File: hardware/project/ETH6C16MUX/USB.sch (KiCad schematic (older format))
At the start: 9 parts

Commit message: Schematic design
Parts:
- L?: symbol ETH6C12MUX:744233121 -> ETH6C16MUX:744233121
- U?: symbol ETH6C12MUX:824011 -> ETH6C16MUX:824011
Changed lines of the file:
@@
 EESchema Schematic File Version 4
-LIBS:ETH6C12MUX-cache
+LIBS:ETH6C16MUX-cache
 EELAYER 30 0
 EELAYER END
@@
 	4000 1950 4000 1900
 $Comp
-L ETH6C12MUX:744233121 L?
+L ETH6C16MUX:744233121 L?
 U 1 1 5D613F1C
 P 5000 2850
@@
 	4800 2750 4150 2750
 $Comp
-L ETH6C12MUX:824011 U?
+L ETH6C16MUX:824011 U?
 U 1 1 5D6092DD
 P 6700 4100
@@
 	6200 1900 6200 1950
 $Comp
-L ETH6C12MUX:V_USB2 #PWR?
+L ETH6C16MUX:V_USB2 #PWR?
 U 1 1 5D64A71D
 P 6700 3800
@@
 	6200 3000 6200 3150
 $Comp
-L ETH6C12MUX:+5V_USB1 #PWR?
+L ETH6C16MUX:+5V_USB1 #PWR?
 U 1 1 5D6B2E7A
 P 4000 1900
@@
 $EndComp
 $Comp
-L ETH6C12MUX:V_USB1 #PWR?
+L ETH6C16MUX:V_USB1 #PWR?
 U 1 1 5D6B3D26
 P 6200 1900

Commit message: USB update
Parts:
- removed R?: 0, symbol Device:R
- added C? (x2): 1u, symbol Device:C
- added C?: 100n, symbol Device:C
- added R? (x2): 27, symbol Device:R
- added R?: 10k, symbol Device:R
- added U?: FT230XQ, Package_DFN_QFN:QFN-16-1EP_4x4mm_P0.65mm_EP2.1x2.1mm, symbol Interface_USB:FT230XQ
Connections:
- net labels added: +5V, +5V_USB, F_USB_D+, F_USB_D-, GND, MCU_RX_UART3, MCU_TX_UART3
- net labels removed: +5V_USB1, USB_ID, USB_VBUS, V_USB1, V_USB2
- wire segments 40 -> 57
- no-connect marks 0 -> 7
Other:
- moved on the sheet: C?, D?, J?, L?, R?, U?

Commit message: Schematic design
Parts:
- C504: renamed from C?; footprint (none) -> ETH6C16MXU:C_0603_A_Pad1.05x0.95mm_HandSolder
- D501: renamed from D?; value D_Schottky -> CUS08F30; footprint (none) -> Diode_SMD:D_SOD-323_HandSoldering
- J501: renamed from J?; footprint (none) -> Connector_USB:USB_Micro-B_Molex-105133-0001
- R501: renamed from R?; value R -> 0/2W
- R502, R503: renamed from R?; footprint (none) -> Resistor_SMD:R_0603_1608Metric_Pad1.05x0.95mm_HandSolder
- U502: renamed from U?; footprint (none) -> Package_TO_SOT_SMD:SOT-23-5
- gave numbers to parts that had none: 8
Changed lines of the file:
@@
 $Descr A4 11693 8268
 encoding utf-8
-Sheet 5 8
+Sheet 5 9
 Title "USB"
 Date ""
@@
 	6650 3500 6200 3500
 $Comp
-L Device:R R?
+L Device:R R503
 U 1 1 5D6EAF5C
 P 6800 3500
-F 0 "R?" V 6700 3500 50  0000 C CNN
+F 0 "R503" V 6700 3500 50  0000 C CNN
 F 1 "27" V 6800 3500 50  0000 C CNN
-F 2 "" V 6730 3500 50  0001 C CNN
+F 2 "Resistor_SMD:R_0603_1608Metric_Pad1.05x0.95mm_HandSolder" V 6730 3500 50  0001 C CNN
 F 3 "~" H 6800 3500 50  0001 C CNN
 	1    6800 3500
@@
 	6650 3300 6200 3300
 $Comp
-L Device:R R?
+L Device:R R502
 U 1 1 5D6EA732
 P 6800 3300
-F 0 "R?" V 6700 3300 50  0000 C CNN
+F 0 "R502" V 6700 3300 50  0000 C CNN
 F 1 "27" V 6800 3300 50  0000 C CNN
-F 2 "" V 6730 3300 50  0001 C CNN
+F 2 "Resistor_SMD:R_0603_1608Metric_Pad1.05x0.95mm_HandSolder" V 6730 3300 50  0001 C CNN
 F 3 "~" H 6800 3300 50  0001 C CNN
 	1    6800 3300
@@
 	7700 3450 7900 3450
 $Comp
-L power:GNDD #PWR?
+L power:GNDD #PWR0511
 U 1 1 5D614548
 P 9050 5000
-F 0 "#PWR?" H 9050 4750 50  0001 C CNN
+F 0 "#PWR0511" H 9050 4750 50  0001 C CNN
 F 1 "GNDD" H 9054 4845 50  0000 C CNN
 F 2 "" H 9050 5000 50  0001 C CNN
@@
 $EndComp
 $Comp
-L ETH6C16MUX:824011 U?
+L ETH6C16MUX:824011 U502
 U 1 1 5D6092DD
 P 9050 4650
-F 0 "U?" H 9328 4671 50  0000 L CNN
+F 0 "U502" H 9328 4671 50  0000 L CNN
 F 1 "824011" H 9328 4580 50  0000 L CNN
-F 2 "" H 8800 4650 50  0001 C CNN
+F 2 "Package_TO_SOT_SMD:SOT-23-5" H 8800 4650 50  0001 C CNN
 F 3 "" H 8800 4650 50  0001 C CNN
 	1    9050 4650
@@
 	7700 3450 7700 3500
 $Comp
-L ETH6C16MUX:744233121 L?
+L ETH6C16MUX:744233121 L502
 U 1 1 5D613F1C
 P 7350 3400
-F 0 "L?" H 7350 3600 50  0000 C CNN
+F 0 "L502" H 7350 3600 50  0000 C CNN
 F 1 "744233121" H 7350 3200 50  0000 C CNN
 F 2 "" H 7350 3400 50  0001 C CNN
@@
 $EndComp
 $Comp
-L Connector:USB_B_Micro J?
+L Connector:USB_B_Micro J501
 U 1 1 5D762E84
 P 9000 3350
-F 0 "J?" H 9057 3817 50  0000 C CNN
+F 0 "J501" H 9057 3817 50  0000 C CNN
 F 1 "105133-0001" H 9057 3726 50  0000 C CNN
-F 2 "" H 9150 3300 50  0001 C CNN
+F 2 "Connector_USB:USB_Micro-B_Molex-105133-0001" H 9150 3300 50  0001 C CNN
 F 3 "~" H 9150 3300 50  0001 C CNN
 	1    9000 3350
@@
 	9000 3800 9000 3750
 $Comp
-L power:GNDD #PWR?
+L power:GNDD #PWR0507
 U 1 1 5D768FA3
 P 9050 3850
-F 0 "#PWR?" H 9050 3600 50  0001 C CNN
+F 0 "#PWR0507" H 9050 3600 50  0001 C CNN
 F 1 "GNDD" H 9054 3695 50  0000 C CNN
 F 2 "" H 9050 3850 50  0001 C CNN
@@
 	6900 2150 6700 2150
 $Comp
-L Device:R R?
+L Device:R R501
 U 1 1 5DBF6D03
 P 7050 2150
-F 0 "R?" V 6843 2150 50  0000 C CNN
-F 1 "R" V 6934 2150 50  0000 C CNN
+F 0 "R501" V 6843 2150 50  0000 C CNN
+F 1 "0/2W" V 6934 2150 50  0000 C CNN
 F 2 "" V 6980 2150 50  0001 C CNN
 F 3 "~" H 7050 2150 50  0001 C CNN
@@
 $EndComp
 $Comp
-L Device:D_Schottky D?
+L Device:D_Schottky D501
 U 1 1 5DBF3C7F
 P 7050 2500
-F 0 "D?" H 7050 2716 50  0000 C CNN
-F 1 "D_Schottky" H 7050 2625 50  0000 C CNN
-F 2 "" H 7050 2500 50  0001 C CNN
+F 0 "D501" H 7050 2716 50  0000 C CNN
+F 1 "CUS08F30" H 7050 2625 50  0000 C CNN
+F 2 "Diode_SMD:D_SOD-323_HandSoldering" H 7050 2500 50  0001 C CNN
 F 3 "~" H 7050 2500 50  0001 C CNN
 	1    7050 2500
@@
 Connection ~ 8050 2500
 $Comp
-L power:GNDD #PWR?
+L power:GNDD #PWR0504
 U 1 1 5D600B45
 P 8050 2850
-F 0 "#PWR?" H 8050 2600 50  0001 C CNN
+F 0 "#PWR0504" H 8050 2600 50  0001 C CNN
 F 1 "GNDD" H 8054 2695 50  0000 C CNN
 F 2 "" H 8050 2850 50  0001 C CNN
@@
 $EndComp
 $Comp
-L power:GNDD #PWR?
+L power:GNDD #PWR0503
 U 1 1 5D600B3F
 P 7450 2850
-F 0 "#PWR?" H 7450 2600 50  0001 C CNN
+F 0 "#PWR0503" H 7450 2600 50  0001 C CNN
 F 1 "GNDD" H 7454 2695 50  0000 C CNN
 F 2 "" H 7450 2850 50  0001 C CNN
@@
 	8050 2550 8050 2500
 $Comp
-L Device:CP C?
+L Device:CP C502
 U 1 1 5D600B35
 P 8050 2700
-F 0 "C?" H 8168 2746 50  0000 L CNN
+F 0 "C502" H 8168 2746 50  0000 L CNN
 F 1 "470u" H 8168 2655 50  0000 L CNN
 F 2 "" H 8088 2550 50  0001 C CNN
@@
 $EndComp
 $Comp
-L Device:L L?
+L Device:L L501
 U 1 1 5D600B2F
 P 7750 2500
-F 0 "L?" V 7940 2500 50  0000 C CNN
+F 0 "L501" V 7940 2500 50  0000 C CNN
 F 1 "744053220" V 7849 2500 50  0000 C CNN
 F 2 "" H 7750 2500 50  0001 C CNN
@@
 $EndComp
 $Comp
-L Device:CP C?
+L Device:CP C501
 U 1 1 5D600B29
 P 7450 2700
-F 0 "C?" H 7568 2746 50  0000 L CNN
+F 0 "C501" H 7568 2746 50  0000 L CNN
 F 1 "470u" H 7568 2655 50  0000 L CNN
 F 2 "" H 7488 2550 50  0001 C CNN
@@
 NoConn ~ 8700 3550
 $Comp
-L Interface_USB:FT230XQ U?
+L Interface_USB:FT230XQ U501
 U 1 1 5D6F3A21
 P 3800 3650
-F 0 "U?" H 3400 4350 50  0000 C CNN
+F 0 "U501" H 3400 4350 50  0000 C CNN
 F 1 "FT230XQ" H 3400 4250 50  0000 C CNN
 F 2 "Package_DFN_QFN:QFN-16-1EP_4x4mm_P0.65mm_EP2.1x2.1mm" H 4350 2950 50  0001 C CNN
@@
 	4850 3650 4500 3650
 $Comp
-L Device:C C?
+L Device:C C505
 U 1 1 5D71767C
 P 1600 7100
-F 0 "C?" H 1715 7146 50  0000 L CNN
+F 0 "C505" H 1715 7146 50  0000 L CNN
 F 1 "1u" H 1715 7055 50  0000 L CNN
 F 2 "" H 1638 6950 50  0001 C CNN
@@
 	3800 4400 3900 4400
 $Comp
-L power:GND #PWR?
+L power:GND #PWR0510
 U 1 1 5D71A5DB
 P 3800 4450
-F 0 "#PWR?" H 3800 4200 50  0001 C CNN
+F 0 "#PWR0510" H 3800 4200 50  0001 C CNN
 F 1 "GND" H 3805 4277 50  0000 C CNN
 F 2 "" H 3800 4450 50  0001 C CNN
@@
 	3700 2550 3700 2950
 $Comp
-L Device:R R?
+L Device:R R504
 U 1 1 5D7279EC
 P 5000 3600
-F 0 "R?" H 4930 3554 50  0000 R CNN
+F 0 "R504" H 4930 3554 50  0000 R CNN
 F 1 "10k" H 4930 3645 50  0000 R CNN
 F 2 "" V 4930 3600 50  0001 C CNN
@@
 Connection ~ 5000 3250
 $Comp
-L Device:C C?
+L Device:C C504
 U 1 1 5D72EA0B
 P 5000 4100
-F 0 "C?" H 5115 4146 50  0000 L CNN
+F 0 "C504" H 5115 4146 50  0000 L CNN
 F 1 "100n" H 5115 4055 50  0000 L CNN
-F 2 "" H 5038 3950 50  0001 C CNN
+F 2 "ETH6C16MXU:C_0603_A_Pad1.05x0.95mm_HandSolder" H 5038 3950 50  0001 C CNN
 F 3 "~" H 5000 4100 50  0001 C CNN
 	1    5000 4100
@@
 Connection ~ 5000 3850
 $Comp
-L power:GND #PWR?
+L power:GND #PWR0508
 U 1 1 5D7314EE
 P 5000 4250
-F 0 "#PWR?" H 5000 4000 50  0001 C CNN
+F 0 "#PWR0508" H 5000 4000 50  0001 C CNN
 F 1 "GND" H 5005 4077 50  0000 C CNN
 F 2 "" H 5000 4250 50  0001 C CNN
@@
 $EndComp
 $Comp
-L Device:C C?
+L Device:C C503
 U 1 1 5D73543E
 P 4550 2750
-F 0 "C?" H 4665 2796 50  0000 L CNN
+F 0 "C503" H 4665 2796 50  0000 L CNN
 F 1 "1u" H 4665 2705 50  0000 L CNN
 F 2 "" H 4588 2600 50  0001 C CNN
@@
 	4550 2550 3700 2550
 $Comp
-L power:GND #PWR?
+L power:GND #PWR0505
 U 1 1 5D739887
 P 4550 2900
-F 0 "#PWR?" H 4550 2650 50  0001 C CNN
+F 0 "#PWR0505" H 4550 2650 50  0001 C CNN
 F 1 "GND" H 4555 2727 50  0000 C CNN
 F 2 "" H 4550 2900 50  0001 C CNN
@@
 NoConn ~ 3100 3550
 $Comp
-L power:GND #PWR?
+L power:GND #PWR0513
 U 1 1 5D76832A
 P 1600 7250
-F 0 "#PWR?" H 1600 7000 50  0001 C CNN
+F 0 "#PWR0513" H 1600 7000 50  0001 C CNN
 F 1 "GND" H 1605 7077 50  0000 C CNN
 F 2 "" H 1600 7250 50  0001 C CNN
@@
 MCU_RX_UART3
 $Comp
-L power:+5V #PWR?
+L power:+5V #PWR0501
 U 1 1 5D78D21A
 P 6350 2450
-F 0 "#PWR?" H 6350 2300 50  0001 C CNN
+F 0 "#PWR0501" H 6350 2300 50  0001 C CNN
 F 1 "+5V" H 6365 2623 50  0000 C CNN
 F 2 "" H 6350 2450 50  0001 C CNN
@@
 $EndComp
 $Comp
-L ETH6C16MUX:+5V_USB #PWR?
+L ETH6C16MUX:+5V_USB #PWR0502
 U 1 1 5D78DEBD
 P 8550 2450
-F 0 "#PWR?" H 8550 2300 50  0001 C CNN
+F 0 "#PWR0502" H 8550 2300 50  0001 C CNN
 F 1 "+5V_USB" H 8565 2623 50  0000 C CNN
 F 2 "" H 8550 2450 50  0001 C CNN
@@
 $EndComp
 $Comp
-L ETH6C16MUX:+5V_USB #PWR?
+L ETH6C16MUX:+5V_USB #PWR0509
 U 1 1 5D78E0EA
 P 9050 4350
-F 0 "#PWR?" H 9050 4200 50  0001 C CNN
+F 0 "#PWR0509" H 9050 4200 50  0001 C CNN
 F 1 "+5V_USB" H 9065 4523 50  0000 C CNN
 F 2 "" H 9050 4350 50  0001 C CNN
@@
 $EndComp
 $Comp
-L power:+5V #PWR?
+L power:+5V #PWR0506
 U 1 1 5D7913F2
 P 3900 2950
-F 0 "#PWR?" H 3900 2800 50  0001 C CNN
+F 0 "#PWR0506" H 3900 2800 50  0001 C CNN
 F 1 "+5V" H 3915 3123 50  0000 C CNN
 F 2 "" H 3900 2950 50  0001 C CNN
@@
 $EndComp
 $Comp
-L power:+5V #PWR?
+L power:+5V #PWR0512
 U 1 1 5D7940E4
 P 1600 6950
-F 0 "#PWR?" H 1600 6800 50  0001 C CNN
+F 0 "#PWR0512" H 1600 6800 50  0001 C CNN
 F 1 "+5V" H 1615 7123 50  0000 C CNN
 F 2 "" H 1600 6950 50  0001 C CNN

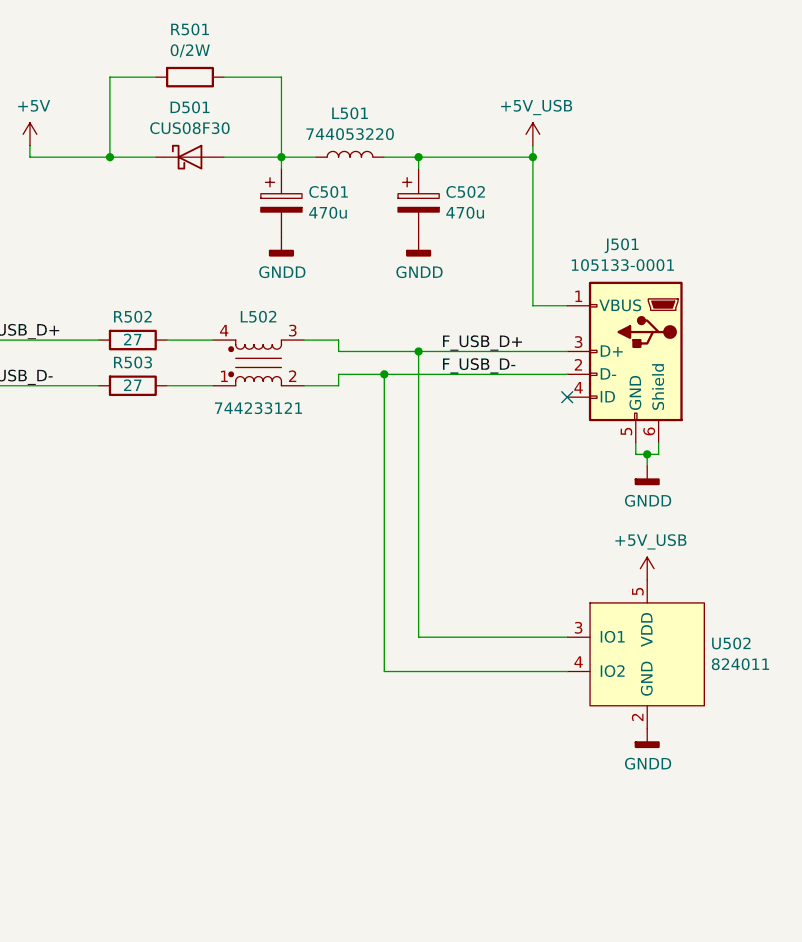
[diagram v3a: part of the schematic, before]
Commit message: PCB design, need to redesign of the board to board connectors.
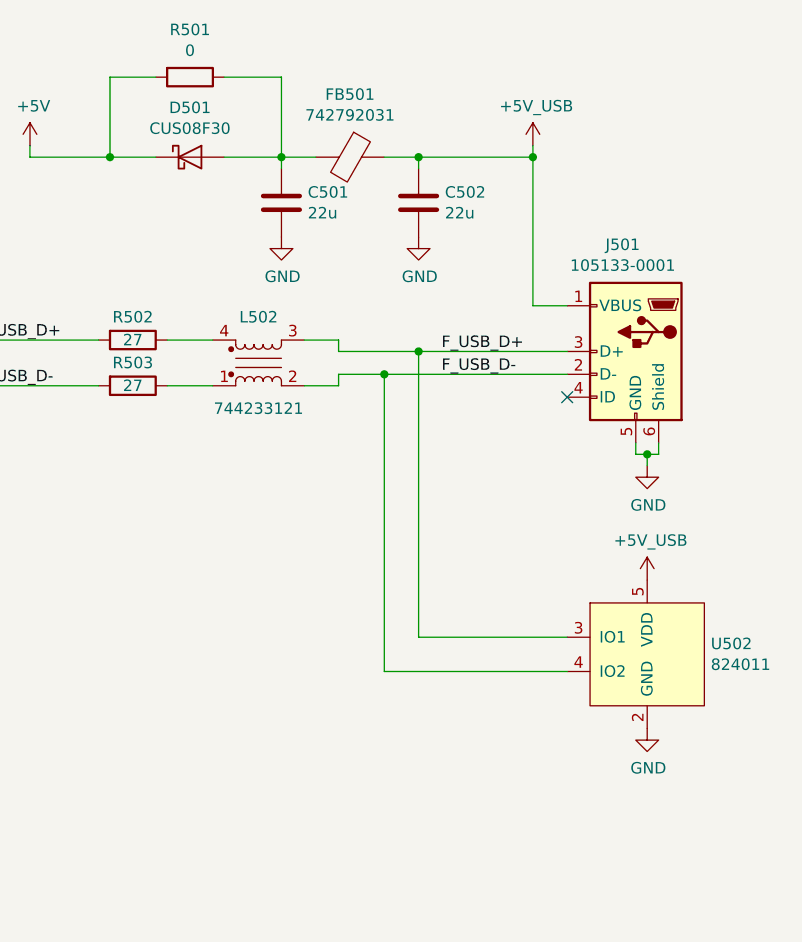
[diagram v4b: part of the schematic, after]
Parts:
- removed C501, C502: 470u, symbol Device:CP
- removed L501: 744053220, symbol Device:L
- added C501, C502: 22u, ETH6C16MXU:C_1210_BB_3225Metric_Pad1.42x2.65mm_HandSolder, symbol Device:C
- added FB501: 742792031, ETH6C16MXU:R_0805_D_Pad1.15x1.40mm_HandSolder, symbol Device:Ferrite_Bead
- C503, C505: footprint (none) -> ETH6C16MXU:C_0603_B_Pad1.05x0.95mm_HandSolder
- L502: footprint (none) -> ETH6C16MXU:744233121
- R501: value 0/2W -> 0; footprint (none) -> Resistor_SMD:R_0612_1632Metric_Pad1.18x3.40mm_HandSolder
- R504: footprint (none) -> ETH6C16MXU:R_0603_E_Pad1.05x0.95mm_HandSolder
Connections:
- net GNDD is gone; now on net GND: J501.5 (GND), J501.6 (Shield), U502.2 (GND)
- net +5V_USB: now also C502.1, FB501.1
- net GND: now also C501.2, C502.2
- net at D501.2 (A), R501.1: now also C501.1, FB501.2
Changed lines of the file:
@@
 	7700 3450 7900 3450
-$Comp
-L power:GNDD #PWR0511
-U 1 1 5D614548
-P 9050 5000
-F 0 "#PWR0511" H 9050 4750 50  0001 C CNN
-F 1 "GNDD" H 9054 4845 50  0000 C CNN
-F 2 "" H 9050 5000 50  0001 C CNN
-F 3 "" H 9050 5000 50  0001 C CNN
-	1    9050 5000
-	1    0    0    -1
-$EndComp
 $Comp
 L ETH6C16MUX:824011 U502
@@
 F 0 "L502" H 7350 3600 50  0000 C CNN
 F 1 "744233121" H 7350 3200 50  0000 C CNN
-F 2 "" H 7350 3400 50  0001 C CNN
+F 2 "ETH6C16MXU:744233121" H 7350 3400 50  0001 C CNN
 F 3 "" H 7350 3400 50  0001 C CNN
 	1    7350 3400
@@
 Wire Wire Line
 	9000 3800 9000 3750
-$Comp
-L power:GNDD #PWR0507
-U 1 1 5D768FA3
-P 9050 3850
-F 0 "#PWR0507" H 9050 3600 50  0001 C CNN
-F 1 "GNDD" H 9054 3695 50  0000 C CNN
-F 2 "" H 9050 3850 50  0001 C CNN
-F 3 "" H 9050 3850 50  0001 C CNN
-	1    9050 3850
-	1    0    0    -1
-$EndComp
 Wire Wire Line
 	9050 3850 9050 3800
@@
 P 7050 2150
 F 0 "R501" V 6843 2150 50  0000 C CNN
-F 1 "0/2W" V 6934 2150 50  0000 C CNN
-F 2 "" V 6980 2150 50  0001 C CNN
+F 1 "0" V 6934 2150 50  0000 C CNN
+F 2 "Resistor_SMD:R_0612_1632Metric_Pad1.18x3.40mm_HandSolder" V 6980 2150 50  0001 C CNN
 F 3 "~" H 7050 2150 50  0001 C CNN
 	1    7050 2150
@@
 	6700 2500 6350 2500
 Connection ~ 8050 2500
-$Comp
-L power:GNDD #PWR0504
-U 1 1 5D600B45
-P 8050 2850
-F 0 "#PWR0504" H 8050 2600 50  0001 C CNN
-F 1 "GNDD" H 8054 2695 50  0000 C CNN
-F 2 "" H 8050 2850 50  0001 C CNN
-F 3 "" H 8050 2850 50  0001 C CNN
-	1    8050 2850
-	1    0    0    -1
-$EndComp
-$Comp
-L power:GNDD #PWR0503
-U 1 1 5D600B3F
-P 7450 2850
-F 0 "#PWR0503" H 7450 2600 50  0001 C CNN
-F 1 "GNDD" H 7454 2695 50  0000 C CNN
-F 2 "" H 7450 2850 50  0001 C CNN
-F 3 "" H 7450 2850 50  0001 C CNN
-	1    7450 2850
-	1    0    0    -1
-$EndComp
 Wire Wire Line
 	7450 2500 7450 2550
@@
 Wire Wire Line
 	8050 2550 8050 2500
-$Comp
-L Device:CP C502
-U 1 1 5D600B35
-P 8050 2700
-F 0 "C502" H 8168 2746 50  0000 L CNN
-F 1 "470u" H 8168 2655 50  0000 L CNN
-F 2 "" H 8088 2550 50  0001 C CNN
-F 3 "~" H 8050 2700 50  0001 C CNN
-	1    8050 2700
-	1    0    0    -1
-$EndComp
-$Comp
-L Device:L L501
-U 1 1 5D600B2F
-P 7750 2500
-F 0 "L501" V 7940 2500 50  0000 C CNN
-F 1 "744053220" V 7849 2500 50  0000 C CNN
-F 2 "" H 7750 2500 50  0001 C CNN
-F 3 "~" H 7750 2500 50  0001 C CNN
-	1    7750 2500
-	0    -1   -1   0
-$EndComp
-$Comp
-L Device:CP C501
-U 1 1 5D600B29
-P 7450 2700
-F 0 "C501" H 7568 2746 50  0000 L CNN
-F 1 "470u" H 7568 2655 50  0000 L CNN
-F 2 "" H 7488 2550 50  0001 C CNN
-F 3 "~" H 7450 2700 50  0001 C CNN
-	1    7450 2700
-	1    0    0    -1
-$EndComp
 NoConn ~ 8700 3550
 $Comp
@@
 F 0 "C505" H 1715 7146 50  0000 L CNN
 F 1 "1u" H 1715 7055 50  0000 L CNN
-F 2 "" H 1638 6950 50  0001 C CNN
+F 2 "ETH6C16MXU:C_0603_B_Pad1.05x0.95mm_HandSolder" H 1638 6950 50  0001 C CNN
 F 3 "~" H 1600 7100 50  0001 C CNN
 	1    1600 7100
@@
 F 0 "R504" H 4930 3554 50  0000 R CNN
 F 1 "10k" H 4930 3645 50  0000 R CNN
-F 2 "" V 4930 3600 50  0001 C CNN
+F 2 "ETH6C16MXU:R_0603_E_Pad1.05x0.95mm_HandSolder" V 4930 3600 50  0001 C CNN
 F 3 "~" H 5000 3600 50  0001 C CNN
 	1    5000 3600
@@
 F 0 "C503" H 4665 2796 50  0000 L CNN
 F 1 "1u" H 4665 2705 50  0000 L CNN
-F 2 "" H 4588 2600 50  0001 C CNN
+F 2 "ETH6C16MXU:C_0603_B_Pad1.05x0.95mm_HandSolder" H 4588 2600 50  0001 C CNN
 F 3 "~" H 4550 2750 50  0001 C CNN
 	1    4550 2750
@@
 	1    0    0    -1
 $EndComp
+$Comp
+L Device:C C?
+U 1 1 61D3CE43
+P 8050 2700
+AR Path="/5D7684C8/61D3CE43" Ref="C?"  Part="1"
+AR Path="/5D737AE2/61D3CE43" Ref="C502"  Part="1"
+F 0 "C502" H 8165 2746 50  0000 L CNN
+F 1 "22u" H 8165 2655 50  0000 L CNN
+F 2 "ETH6C16MXU:C_1210_BB_3225Metric_Pad1.42x2.65mm_HandSolder" H 8088 2550 50  0001 C CNN
+F 3 "~" H 8050 2700 50  0001 C CNN
+	1    8050 2700
+	1    0    0    -1
+$EndComp
+$Comp
+L Device:C C?
+U 1 1 61D3E0E2
+P 7450 2700
+AR Path="/5D7684C8/61D3E0E2" Ref="C?"  Part="1"
+AR Path="/5D737AE2/61D3E0E2" Ref="C501"  Part="1"
+F 0 "C501" H 7565 2746 50  0000 L CNN
+F 1 "22u" H 7565 2655 50  0000 L CNN
+F 2 "ETH6C16MXU:C_1210_BB_3225Metric_Pad1.42x2.65mm_HandSolder" H 7488 2550 50  0001 C CNN
+F 3 "~" H 7450 2700 50  0001 C CNN
+	1    7450 2700
+	1    0    0    -1
+$EndComp
+$Comp
+L Device:Ferrite_Bead FB?
+U 1 1 61D4304C
+P 7750 2500
+AR Path="/5D7684C8/61D4304C" Ref="FB?"  Part="1"
+AR Path="/5D737AE2/61D4304C" Ref="FB501"  Part="1"
+F 0 "FB501" V 7476 2500 50  0000 C CNN
+F 1 "742792031" V 7567 2500 50  0000 C CNN
+F 2 "ETH6C16MXU:R_0805_D_Pad1.15x1.40mm_HandSolder" V 7680 2500 50  0001 C CNN
+F 3 "~" H 7750 2500 50  0001 C CNN
+	1    7750 2500
+	0    1    1    0
+$EndComp
+$Comp
+L power:GND #PWR0137
+U 1 1 61DC20ED
+P 9050 3850
+F 0 "#PWR0137" H 9050 3600 50  0001 C CNN
+F 1 "GND" H 9055 3677 50  0000 C CNN
+F 2 "" H 9050 3850 50  0001 C CNN
+F 3 "" H 9050 3850 50  0001 C CNN
+	1    9050 3850
+	1    0    0    -1
+$EndComp
+$Comp
+L power:GND #PWR0138
+U 1 1 61DC2D16
+P 9050 5000
+F 0 "#PWR0138" H 9050 4750 50  0001 C CNN
+F 1 "GND" H 9055 4827 50  0000 C CNN
+F 2 "" H 9050 5000 50  0001 C CNN
+F 3 "" H 9050 5000 50  0001 C CNN
+	1    9050 5000
+	1    0    0    -1
+$EndComp
+$Comp
+L power:GND #PWR0139
+U 1 1 61DC3367
+P 7450 2850
+F 0 "#PWR0139" H 7450 2600 50  0001 C CNN
+F 1 "GND" H 7455 2677 50  0000 C CNN
+F 2 "" H 7450 2850 50  0001 C CNN
+F 3 "" H 7450 2850 50  0001 C CNN
+	1    7450 2850
+	1    0    0    -1
+$EndComp
+$Comp
+L power:GND #PWR0140
+U 1 1 61DC47AE
+P 8050 2850
+F 0 "#PWR0140" H 8050 2600 50  0001 C CNN
+F 1 "GND" H 8055 2677 50  0000 C CNN
+F 2 "" H 8050 2850 50  0001 C CNN
+F 3 "" H 8050 2850 50  0001 C CNN
+	1    8050 2850
+	1    0    0    -1
+$EndComp
